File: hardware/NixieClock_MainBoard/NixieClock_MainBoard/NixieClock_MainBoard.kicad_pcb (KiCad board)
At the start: 2 copper layers, 152.4 x 63.5 mm, 6 parts, among them J1 Conn_01x14, J2 Conn_01x08, J3 Conn_01x08, J4 Conn_01x08, J5 Conn_01x08, U1 ESP32-WROOM-32E

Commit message: update: mainboard sheet
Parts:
- added J6: USB_C_Receptacle_USB2.0_16P, Connector_USB:USB_C_Receptacle_G-Switch_GT-USB-7010ASV, B.Cu at (173.0, 78.8)
- added U2: FT220XS, Package_QFP:LQFP-48_7x7mm_P0.5mm, B.Cu at (166.8, 96.7)
- added U3: R-78C3.3-1.0, Converter_DCDC:Converter_DCDC_RECOM_R-78E-0.5_THT, B.Cu at (179.4, 99.1)
- added U4: PCA9547D, Package_SO:SOIC-24W_7.5x15.4mm_P1.27mm, B.Cu at (77.9, 101.3)

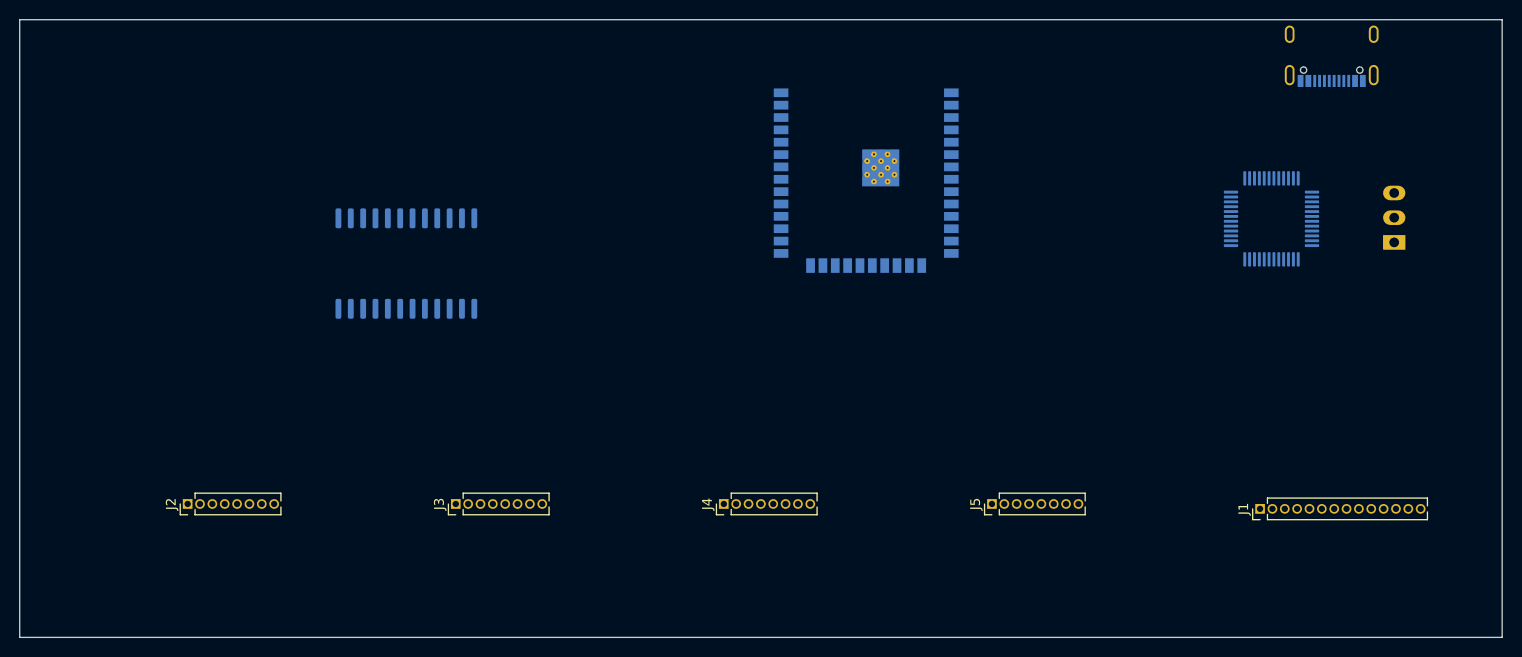
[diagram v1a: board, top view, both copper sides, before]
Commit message: add mainboard schematic
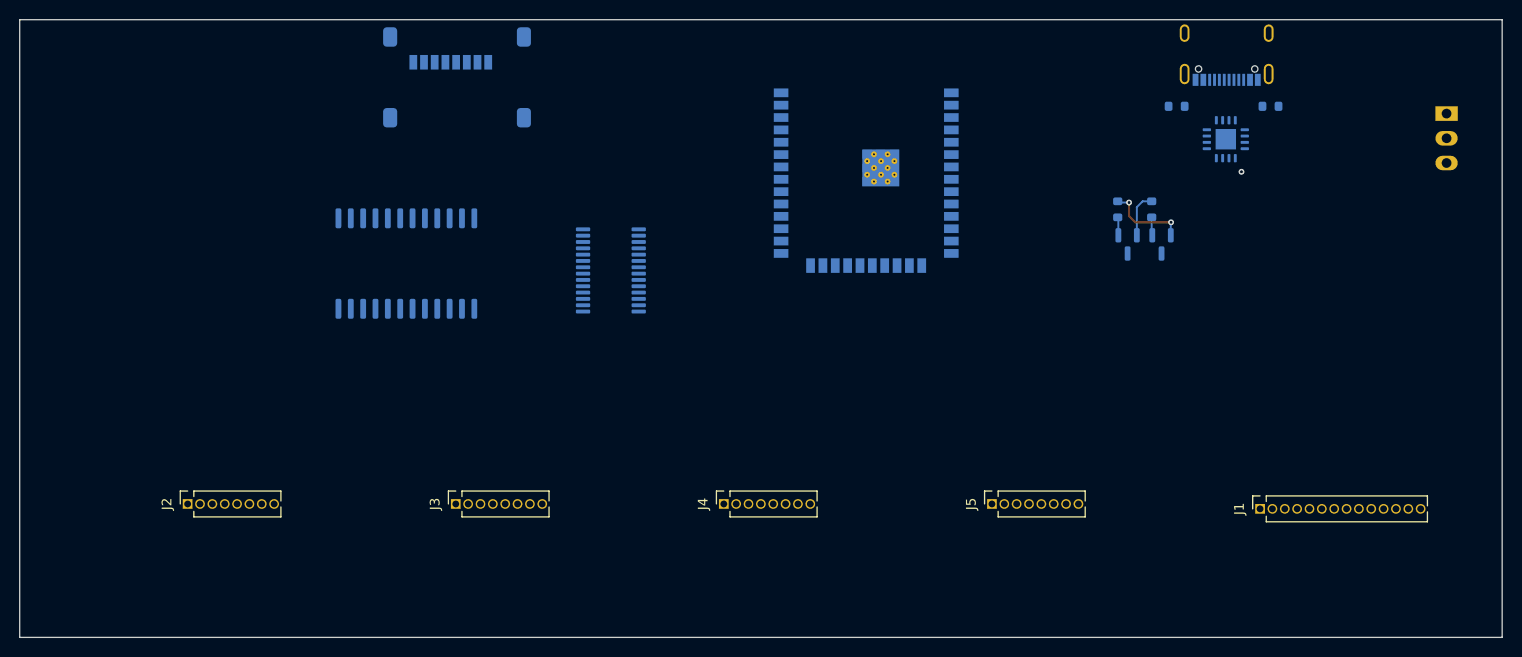
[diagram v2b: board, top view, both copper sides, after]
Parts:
- added J7: Micro_SD_Card, Connector_Card:microSD_HC_Molex_47219-2001, B.Cu at (83.1, 82.7)
- added Q1: BC847, Package_TO_SOT_SMD:SOT-23, B.Cu at (152.0, 99.3)
- added Q2: BC847, Package_TO_SOT_SMD:SOT-23, B.Cu at (155.5, 99.3)
- added R1: 5k1, Resistor_SMD:R_0603_1608Metric, B.Cu at (157.0, 85.1)
- added R2: 5k1, Resistor_SMD:R_0603_1608Metric, B.Cu at (166.7, 85.1)
- added R3: 12k, Resistor_SMD:R_0603_1608Metric, B.Cu at (151.0, 95.7)
- added R4: 12k, Resistor_SMD:R_0603_1608Metric, B.Cu at (154.5, 95.7)
- added U5: PCA9635, Package_SO:TSSOP-28_4.4x9.7mm_P0.65mm, B.Cu at (98.9, 102.0)
- J1: footprint Connector_PinHeader_1.27mm:PinHeader_1x14_P1.27mm_Vertical -> Connector_PinSocket_1.27mm:PinSocket_1x14_P1.27mm_Vertical
- J2, J3, J4, J5: footprint Connector_PinHeader_1.27mm:PinHeader_1x08_P1.27mm_Vertical -> Connector_PinSocket_1.27mm:PinSocket_1x08_P1.27mm_Vertical
- U2: value FT220XS -> R-78C3.3-1.0; footprint Package_QFP:LQFP-48_7x7mm_P0.5mm -> Converter_DCDC:Converter_DCDC_RECOM_R-78E-0.5_THT
- U3: value R-78C3.3-1.0 -> FT230XQ; footprint Converter_DCDC:Converter_DCDC_RECOM_R-78E-0.5_THT -> Package_DFN_QFN:QFN-16-1EP_4x4mm_P0.65mm_EP2.1x2.1mm
- moved U2 21.0 mm to (184.8, 85.9), turned to -90 degrees
- moved U3 20.3 mm to (162.1, 88.5), turned to 0 degrees
- moved J6 10.8 mm to (162.2, 78.7)
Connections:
- J1 pad 13: /GND -> GND
- J1 pad 2: /GND -> GND
- J1 pad 5: /GND -> GND
- J2 pad 2: /GND -> GND
- J3 pad 2: /GND -> GND
- J4 pad 2: /GND -> GND
- J5 pad 2: /GND -> GND
- J6 pad A1: Net-(J6-GND-PadA1) -> GND
- J6 pad A12: Net-(J6-GND-PadA1) -> GND
- J6 pad A4: Net-(J6-VBUS-PadA4) -> Net-(U2-IN)
- J6 pad A5: unconnected-(J6-CC1-PadA5) -> Net-(J6-CC1)
- J6 pad A6: unconnected-(J6-D+-PadA6) -> Net-(U3-USBDP)
- J6 pad A7: unconnected-(J6-D--PadA7) -> Net-(U3-USBDM)
- J6 pad A9: Net-(J6-VBUS-PadA4) -> Net-(U2-IN)
- J6 pad B1: Net-(J6-GND-PadA1) -> GND
- J6 pad B12: Net-(J6-GND-PadA1) -> GND
- J6 pad B4: Net-(J6-VBUS-PadA4) -> Net-(U2-IN)
- J6 pad B5: unconnected-(J6-CC2-PadB5) -> Net-(J6-CC2)
- J6 pad B6: unconnected-(J6-D+-PadB6) -> Net-(U3-USBDP)
- J6 pad B7: unconnected-(J6-D--PadB7) -> Net-(U3-USBDM)
- J6 pad B9: Net-(J6-VBUS-PadA4) -> Net-(U2-IN)
- J6 pad S1: unconnected-(J6-SHIELD-PadS1) -> GND
- U1 pad 1: Net-(U1-GND-Pad1) -> GND
- U1 pad 10: unconnected-(U1-IO25-Pad10) -> /PWM_1
- U1 pad 11: unconnected-(U1-IO26-Pad11) -> /DISP_POWER_EN
- U1 pad 12: unconnected-(U1-IO27-Pad12) -> /PWM2
- U1 pad 14: /CS_3 -> unconnected-(U1-IO12-Pad14)
- U1 pad 15: Net-(U1-GND-Pad1) -> GND
- U1 pad 25: unconnected-(U1-IO0-Pad25) -> /IO0
- U1 pad 26: unconnected-(U1-IO4-Pad26) -> /CS_MEM_1
- U1 pad 29: unconnected-(U1-IO5-Pad29) -> /CS_3
- U1 pad 3: unconnected-(U1-EN-Pad3) -> /EN
- U1 pad 33: unconnected-(U1-IO21-Pad33) -> /SDA
- U1 pad 34: unconnected-(U1-RXD0/IO3-Pad34) -> /MCU_RXD
- U1 pad 35: unconnected-(U1-TXD0/IO1-Pad35) -> /MCU_TXD
- U1 pad 36: unconnected-(U1-IO22-Pad36) -> /SCL
- U1 pad 38: Net-(U1-GND-Pad1) -> GND
- U1 pad 39: Net-(U1-GND-Pad1) -> GND
- U1 pad 8: unconnected-(U1-IO32-Pad8) -> /WakeUp_1
- U1 pad 9: unconnected-(U1-IO33-Pad9) -> /WakeUp_2
- U2 pad 1: unconnected-(U2-MIOSI0-Pad1) -> Net-(U2-IN)
- U2 pad 2: unconnected-(U2-MIOSI2-Pad2) -> GND
- U2 pad 3: unconnected-(U2-VCCIO-Pad3) -> +3.3V
- U3 pad 1: unconnected-(U3-IN-Pad1) -> +3.3V
- U3 pad 2: unconnected-(U3-GND-Pad2) -> /MCU_TXD
- U3 pad 3: unconnected-(U3-OUT-Pad3) -> GND
- U4 pad 12: unconnected-(U4-GND-Pad12) -> GND
- U4 pad 22: unconnected-(U4-SCL-Pad22) -> /SCL
- U4 pad 23: unconnected-(U4-SDA-Pad23) -> /SDA
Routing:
- net /POWER_USB/DTR: track 0.00 -> 8.54 mm, vias 0 -> 2
- net /POWER_USB/RTS: track 0.00 -> 4.67 mm
- net Net-(Q1-B): track 0.00 -> 1.87 mm
- net Net-(Q2-B): track 0.00 -> 1.87 mm
- net GND: vias 0 -> 1

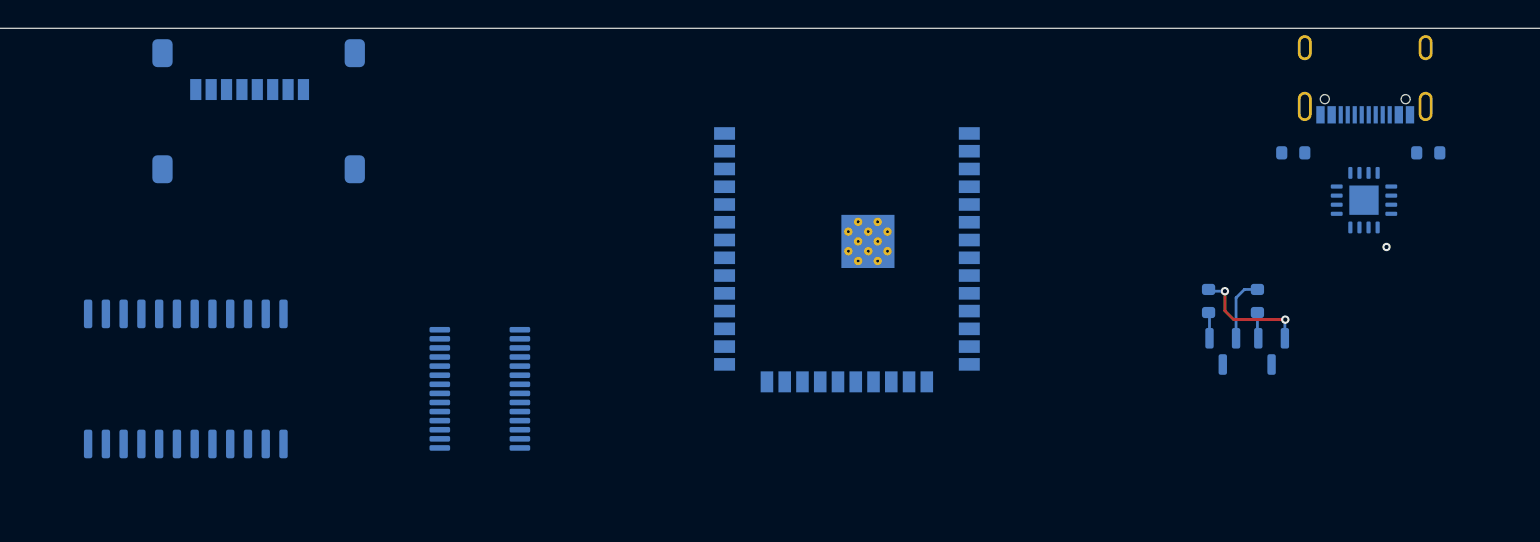
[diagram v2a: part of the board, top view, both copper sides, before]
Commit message: update pcb. distance between fpc-connector corrected
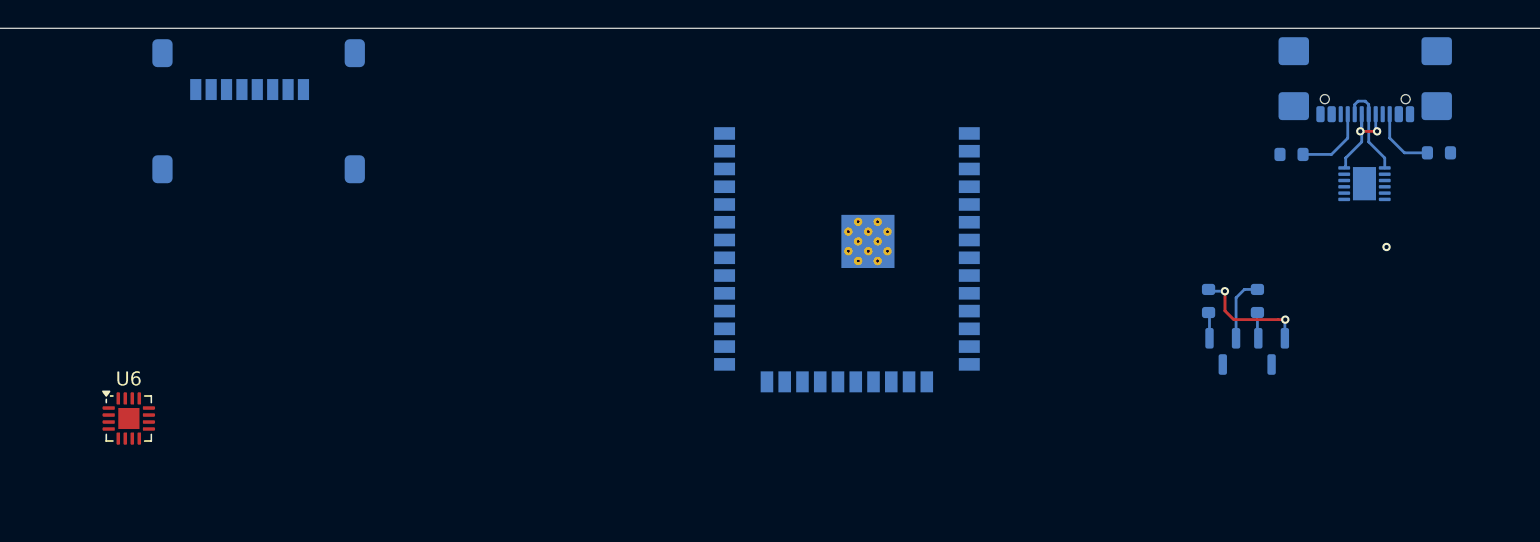
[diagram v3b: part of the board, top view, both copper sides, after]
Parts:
- removed U4: PCA9547D, Package_SO:SOIC-24W_7.5x15.4mm_P1.27mm
- removed U5: PCA9635, Package_SO:TSSOP-28_4.4x9.7mm_P0.65mm
- added U6: PCA9583A, Package_DFN_QFN:HVQFN-16-1EP_3x3mm_P0.5mm_EP1.5x1.5mm, F.Cu at (73.8, 104.1)
- J6: footprint Connector_USB:USB_C_Receptacle_G-Switch_GT-USB-7010ASV -> Connector_USB:USB_C_Receptacle_GCT_USB4110
- U3: value FT230XQ -> FT234XD; footprint Package_DFN_QFN:QFN-16-1EP_4x4mm_P0.65mm_EP2.1x2.1mm -> Package_DFN_QFN:DFN-12-1EP_3x3mm_P0.45mm_EP1.65x2.38mm
- moved R1 10.4 mm to (167.4, 85.1), turned to 0 degrees
- moved R2 9.78 mm to (156.9, 85.2), turned to 180 degrees
- moved U3 1.18 mm to (162.1, 87.3), turned to 180 degrees
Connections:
- U3 pad 1: +3.3V -> Net-(U3-USBDM)
- U3 pad 10: +3.3V -> /MCU_TXD
- U3 pad 12: unconnected-(U3-CBUS0-Pad12) -> Net-(U3-USBDP)
- U3 pad 13: GND -> (no net)
- U3 pad 2: /MCU_TXD -> unconnected-(U3-~{RESET}-Pad2)
- U3 pad 3: GND -> unconnected-(U3-3V3OUT-Pad3)
- U3 pad 4: unconnected-(U3-~{CTS}-Pad4) -> +3.3V
- U3 pad 5: unconnected-(U3-CBUS2-Pad5) -> GND
- U3 pad 6: Net-(U3-USBDP) -> unconnected-(U3-CBUS0-Pad6)
- U3 pad 7: Net-(U3-USBDM) -> /MCU_RXD
- U3 pad 9: unconnected-(U3-~{RESET}-Pad9) -> +3.3V
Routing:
- net Net-(U3-USBDP): track 0.00 -> 8.10 mm, vias 0 -> 2
- net Net-(U3-USBDM): track 0.00 -> 6.89 mm
- net Net-(J6-CC1): track 0.00 -> 5.39 mm
- net Net-(J6-CC2): track 0.00 -> 4.84 mm

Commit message: layout mainboard
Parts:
- added C1: 100nF, Capacitor_SMD:C_0603_1608Metric, B.Cu at (137.8, 84.7)
- added C10: 1u0, Capacitor_SMD:C_0603_1608Metric, B.Cu at (55.6, 96.0)
- added C2: 1u0, Capacitor_SMD:C_0603_1608Metric, B.Cu at (140.6, 84.8)
- added C3: 100nF, Capacitor_SMD:C_0603_1608Metric, B.Cu at (109.2, 96.5)
- added C4: 1u0, Capacitor_SMD:C_0603_1608Metric, B.Cu at (106.7, 96.5)
- added C5: 100nF, Capacitor_SMD:C_0603_1608Metric, B.Cu at (82.3, 92.0)
- added C6: 1u0, Capacitor_SMD:C_0603_1608Metric, B.Cu at (82.3, 94.5)
- added C7: 100nF, Capacitor_SMD:C_0603_1608Metric, B.Cu at (57.3, 81.0)
- added C8: 1u0, Capacitor_SMD:C_0603_1608Metric, B.Cu at (57.3, 83.5)
- added C9: 100nF, Capacitor_SMD:C_0603_1608Metric, B.Cu at (53.8, 96.0)
- added J8: Conn_01x08, Connector_PinHeader_2.54mm:PinHeader_1x08_P2.54mm_Vertical, B.Cu at (43.2, 99.1)
- added J9: Conn_01x03, Connector_PinHeader_2.54mm:PinHeader_1x03_P2.54mm_Vertical, B.Cu at (43.2, 110.5)
- added R10: 10k, Resistor_SMD:R_0603_1608Metric, B.Cu at (139.0, 98.9)
- added R11: 10k, Resistor_SMD:R_0603_1608Metric, B.Cu at (129.6, 106.7)
- added R12: 10k, Resistor_SMD:R_0603_1608Metric, B.Cu at (109.5, 103.1)
- added R13: 10k, Resistor_SMD:R_0603_1608Metric, B.Cu at (87.1, 122.2)
- added R14: 10k, Resistor_SMD:R_0603_1608Metric, B.Cu at (85.5, 122.2)
- added R15: 10k, Resistor_SMD:R_0603_1608Metric, B.Cu at (114.7, 122.2)
- added R16: 10k, Resistor_SMD:R_0603_1608Metric, B.Cu at (113.0, 122.2)
- added R17: 10k, Resistor_SMD:R_0603_1608Metric, B.Cu at (142.4, 122.2)
- added R18: 10k, Resistor_SMD:R_0603_1608Metric, B.Cu at (140.6, 122.2)
- added R19: 10k, Resistor_SMD:R_0603_1608Metric, B.Cu at (171.4, 122.1)
- added R20: 10k, Resistor_SMD:R_0603_1608Metric, B.Cu at (173.2, 122.1)
- added R21: 10k, Resistor_SMD:R_0603_1608Metric, B.Cu at (177.7, 122.1)
- added R5: 10k, Resistor_SMD:R_0603_1608Metric, B.Cu at (110.6, 90.0)
- added R6: 10k, Resistor_SMD:R_0603_1608Metric, B.Cu at (110.6, 86.1)
- added R7: 10k, Resistor_SMD:R_0603_1608Metric, B.Cu at (57.9, 122.2)
- added R8: 10k, Resistor_SMD:R_0603_1608Metric, B.Cu at (59.6, 122.2)
- added R9: 10k, Resistor_SMD:R_0603_1608Metric, B.Cu at (120.7, 106.6)
- added U10: NC7SZ125M5X, Package_TO_SOT_SMD:SOT-23-5, B.Cu at (106.2, 111.3)
- added U11: NC7SZ125M5X, Package_TO_SOT_SMD:SOT-23-5, B.Cu at (169.6, 107.8)
- added U12: NC7SZ125M5X, Package_TO_SOT_SMD:SOT-23-5, B.Cu at (175.7, 107.8)
- added U4: PCA9635, Package_SO:TSSOP-28_4.4x9.7mm_P0.65mm, B.Cu at (100.3, 98.7)
- added U5: NC7SZ125M5X, Package_TO_SOT_SMD:SOT-23-5, B.Cu at (92.5, 111.3)
- added U7: NC7SZ125M5X, Package_TO_SOT_SMD:SOT-23-5, B.Cu at (96.0, 107.1)
- added U8: NC7SZ125M5X, Package_TO_SOT_SMD:SOT-23-5, B.Cu at (99.4, 111.2)
- added U9: NC7SZ125M5X, Package_TO_SOT_SMD:SOT-23-5, B.Cu at (102.8, 107.1)
- U6: moved to B.Cu
- moved U6 24.6 mm to (53.5, 90.3), turned to 90 degrees
- moved Q1 5.48 mm to (157.4, 98.6)
- moved Q2 5.48 mm to (160.9, 98.6)
- moved R3 5.48 mm to (156.4, 94.9)
- moved R4 5.48 mm to (159.9, 94.9)
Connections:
- net /WakeUp_1 renamed /uC/WakeUp_1
- net /WakeUp_2 renamed /uC/WakeUp_2
- J1 pad 1: /NC -> unconnected-(J1-Pin_1-Pad1)
- J1 pad 14: /NC. -> unconnected-(J1-Pin_14-Pad14)
- J1 pad 3: /LED- -> GND
- J1 pad 4: /LED+ -> /LED_PWM_4
- J1 pad 6: //RES -> Net-(J1-Pin_6)
- J1 pad 7: /A0 -> Net-(J1-Pin_7)
- J2 pad 1: /LEDA -> /LED_PWM_0
- J2 pad 3: /RESET -> Net-(J2-Pin_3)
- J2 pad 4: /RS -> Net-(J2-Pin_4)
- J3 pad 1: /LEDA -> /LED_PWM_1
- J3 pad 3: /RESET -> Net-(J3-Pin_3)
- J3 pad 4: /RS -> Net-(J3-Pin_4)
- J4 pad 1: /LEDA -> /LED_PWM_2
- J4 pad 3: /RESET -> Net-(J4-Pin_3)
- J4 pad 4: /RS -> Net-(J4-Pin_4)
- J5 pad 1: /LEDA -> /LED_PWM_3
- J5 pad 3: /RESET -> Net-(J5-Pin_3)
- J5 pad 4: /RS -> Net-(J5-Pin_4)
- U1 pad 10: /PWM_1 -> /RS
- U1 pad 12: /PWM2 -> unconnected-(U1-IO27-Pad12)
- U1 pad 2: unconnected-(U1-VDD-Pad2) -> +3.3V
- U1 pad 24: //RESET -> /~{RESET}
- U6 pad 1: unconnected-(U6-A0-Pad1) -> GND
- U6 pad 10: unconnected-(U6-IO0_5-Pad10) -> Net-(J8-Pin_8)
- U6 pad 13: unconnected-(U6-~{INT}-Pad13) -> /~{INT_IO}
- U6 pad 16: unconnected-(U6-VDD-Pad16) -> +3.3V
- U6 pad 2: unconnected-(U6-A1-Pad2) -> GND
- U6 pad 3: unconnected-(U6-~{RESET}-Pad3) -> +3.3V
- U6 pad 4: unconnected-(U6-IO0_0-Pad4) -> Net-(J8-Pin_3)
- U6 pad 5: unconnected-(U6-IO0_1-Pad5) -> Net-(J8-Pin_4)
- U6 pad 6: unconnected-(U6-IO0_2-Pad6) -> Net-(J8-Pin_5)
- U6 pad 7: unconnected-(U6-IO0_3-Pad7) -> Net-(J8-Pin_6)
- U6 pad 9: unconnected-(U6-IO0_4-Pad9) -> Net-(J8-Pin_7)
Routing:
- net /MISO: track 0.00 -> 44.5 mm, vias 0 -> 2
- net /SCLK: track 0.00 -> 41.9 mm, vias 0 -> 2
- net /CS_MEM_1: track 0.00 -> 39.8 mm, vias 0 -> 2
- net /MOSI: track 0.00 -> 34.8 mm
- net +3.3V: track 0.00 -> 31.9 mm
- net /SCL: track 0.00 -> 20.3 mm
- net /SDA: track 0.00 -> 16.4 mm
- net GND: track 0.00 -> 15.3 mm
- net Net-(J8-Pin_8): track 0.00 -> 14.5 mm
- net Net-(U4-LED4): track 0.00 -> 13.5 mm
- net Net-(J8-Pin_7): track 0.00 -> 12.9 mm
- net Net-(U10-A): track 0.00 -> 12.2 mm
- net Net-(J8-Pin_3): track 0.00 -> 11.0 mm
- net Net-(J8-Pin_6): track 0.00 -> 10.4 mm
- net Net-(J8-Pin_5): track 0.00 -> 9.54 mm
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
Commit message: update mainboard
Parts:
- removed U3: FT234XD, Package_DFN_QFN:DFN-12-1EP_3x3mm_P0.45mm_EP1.65x2.38mm
- added C11: 100nF, Capacitor_SMD:C_0603_1608Metric, B.Cu at (179.6, 103.6)
- added C12: 100nF, Capacitor_SMD:C_0603_1608Metric, B.Cu at (163.6, 86.9)
- added C13: 1u0, Capacitor_SMD:C_0603_1608Metric, B.Cu at (161.9, 86.9)
- added C14: 100nF, Capacitor_SMD:C_0603_1608Metric, B.Cu at (186.9, 95.7)
- added C15: 1u0, Capacitor_SMD:C_0603_1608Metric, B.Cu at (184.4, 95.7)
- added C16: 100nF, Capacitor_SMD:C_0603_1608Metric, B.Cu at (184.4, 92.6)
- added C17: 1u0, Capacitor_SMD:C_0603_1608Metric, B.Cu at (186.9, 92.6)
- added JP1: SolderJumper_3_Open, Jumper:SolderJumper-3_P1.3mm_Open_Pad1.0x1.5mm, B.Cu at (182.4, 111.5)
- added R22: 10k, Resistor_SMD:R_0603_1608Metric, B.Cu at (138.4, 99.1)
- added R23: 12k, Resistor_SMD:R_0603_1608Metric, B.Cu at (163.3, 90.3)
- added U13: NC7SZ125M5X, Package_TO_SOT_SMD:SOT-23-5, B.Cu at (182.5, 103.9)
- added U14: CP2102N-Axx-xQFN24, Package_DFN_QFN:QFN-24-1EP_4x4mm_P0.5mm_EP2.6x2.6mm, B.Cu at (159.4, 91.0)
- added U15: CH340C, Package_SO:SOIC-16_3.9x9.9mm_P1.27mm, B.Cu at (168.3, 90.9)
- moved J9 143.8 mm to (186.9, 107.8)
- moved C3 37.0 mm to (73.2, 104.8)
- moved C4 36.2 mm to (71.5, 104.9)
- moved U5 35.2 mm to (57.5, 115.0)
- moved U10 35.2 mm to (71.2, 115.0)
- moved U8 35.2 mm to (64.3, 115.0)
- moved U9 35.2 mm to (67.8, 110.8)
- moved U7 35.2 mm to (60.9, 110.8)
- moved U4 35.2 mm to (65.3, 102.5)
- moved R10 26.4 mm to (112.6, 97.7), turned to 0 degrees
- moved R12 20.1 mm to (129.5, 105.3), turned to 90 degrees
- moved R9 14.0 mm to (112.6, 95.1), turned to 0 degrees
- moved R11 10.2 mm to (119.4, 106.3)
- moved Q2 7.68 mm to (153.5, 100.5), turned to 180 degrees
- moved U2 7.54 mm to (180.1, 91.8)
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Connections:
- net Net-(U2-IN) renamed +5V
- J2 pad 6: /SCLk -> /SCLK
- J4 pad 6: /SCLk -> /SCLK
- J7 pad 9: unconnected-(J7-SHIELD-Pad9) -> GND
- J9 pad 1: unconnected-(J9-Pin_1-Pad1) -> Net-(J9-Pin_1)
- J9 pad 2: unconnected-(J9-Pin_2-Pad2) -> Net-(J9-Pin_2)
- J9 pad 3: unconnected-(J9-Pin_3-Pad3) -> GND
- U1 pad 12: unconnected-(U1-IO27-Pad12) -> /WS28XX
- U1 pad 13: /CS_1 -> /CS_4
- U1 pad 16: /CS_2 -> /CS_3
- U1 pad 23: /CS_0 -> /~{RESET}
- U1 pad 24: /~{RESET} -> /CS_2
- U1 pad 27: /CS_4 -> /CS_1
- U1 pad 29: /CS_3 -> /CS_0
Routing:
- net +3.3V: track 31.9 -> 405.7 mm, vias 0 -> 8
- net /MOSI: track 34.8 -> 221.7 mm, vias 0 -> 6
- net /SCLK: track 41.9 -> 223.1 mm, vias 2 -> 8
- net /VDD: track 0.00 -> 153.3 mm, vias 0 -> 5
- net /~{RESET}: track 0.00 -> 151.1 mm, vias 0 -> 2
- net /RS: track 0.00 -> 122.2 mm, vias 0 -> 2
- net /LED_PWM_4: track 0.00 -> 105.3 mm
- net GND: track 15.3 -> 102.4 mm, vias 1 -> 122
- net +5V: track 0.00 -> 85.0 mm, vias 0 -> 1
- net /LED_PWM_3: track 0.00 -> 81.4 mm
- net /CS_0: track 0.00 -> 76.5 mm, vias 0 -> 1
- net /CS_4: track 0.00 -> 69.2 mm, vias 0 -> 2
- net /MCU_TXD: track 0.00 -> 57.8 mm, vias 0 -> 3
- net /SDA: track 16.4 -> 74.2 mm, vias 0 -> 2
- net /MCU_RXD: track 0.00 -> 57.8 mm, vias 0 -> 3
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- added copper zone on B.Cu, net GND
- added copper zone on F.Cu, net GND
